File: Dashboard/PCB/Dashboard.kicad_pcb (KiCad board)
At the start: 4 copper layers, 95.9 x 92.1 mm, 90 parts, among them J1 Display, J2 Conn_01x26_Female, J3 LED, J7 PROGRAMMER, SW1 SW_SPST, U1 STM32F767ZIT6, U10 24LC01, U3 MP2359DJ-LF-Z, U4 AS4C1M16S-6TCN, U5 AT25SF128A-SHB-T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

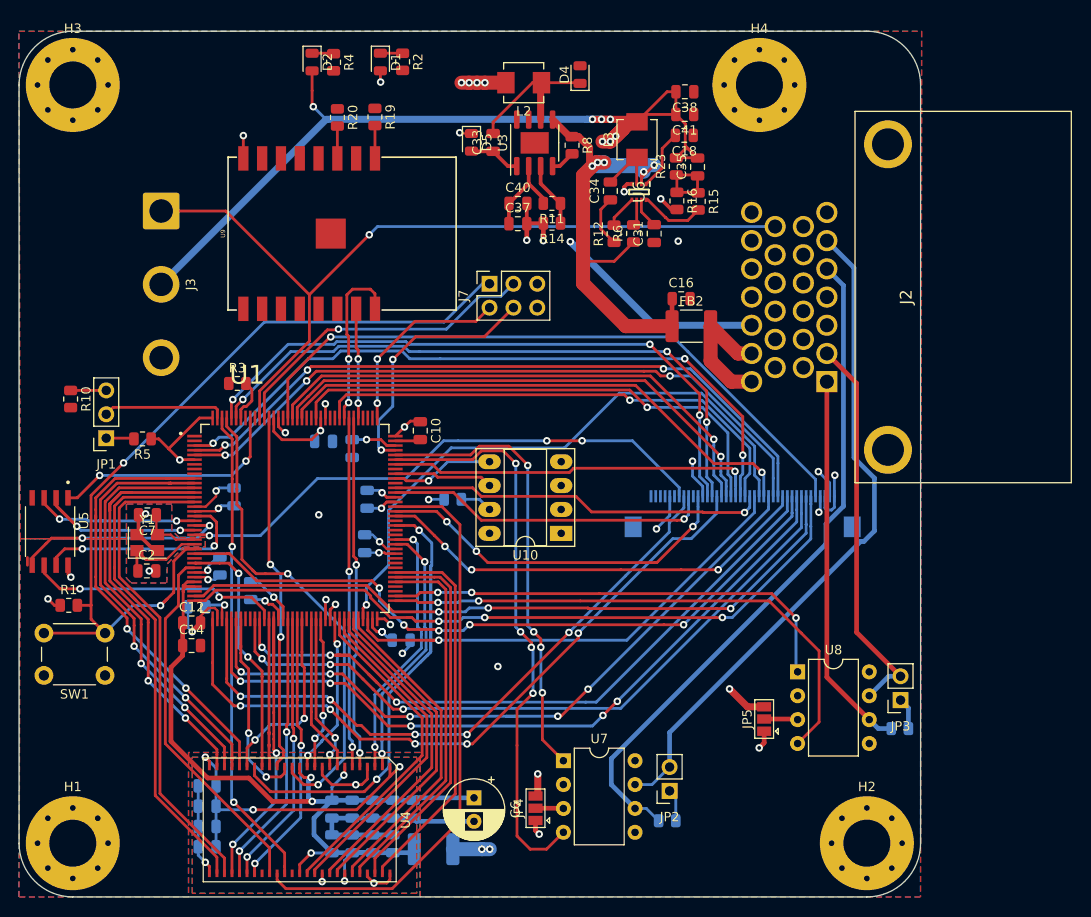
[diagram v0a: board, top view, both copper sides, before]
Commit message: Add signal led
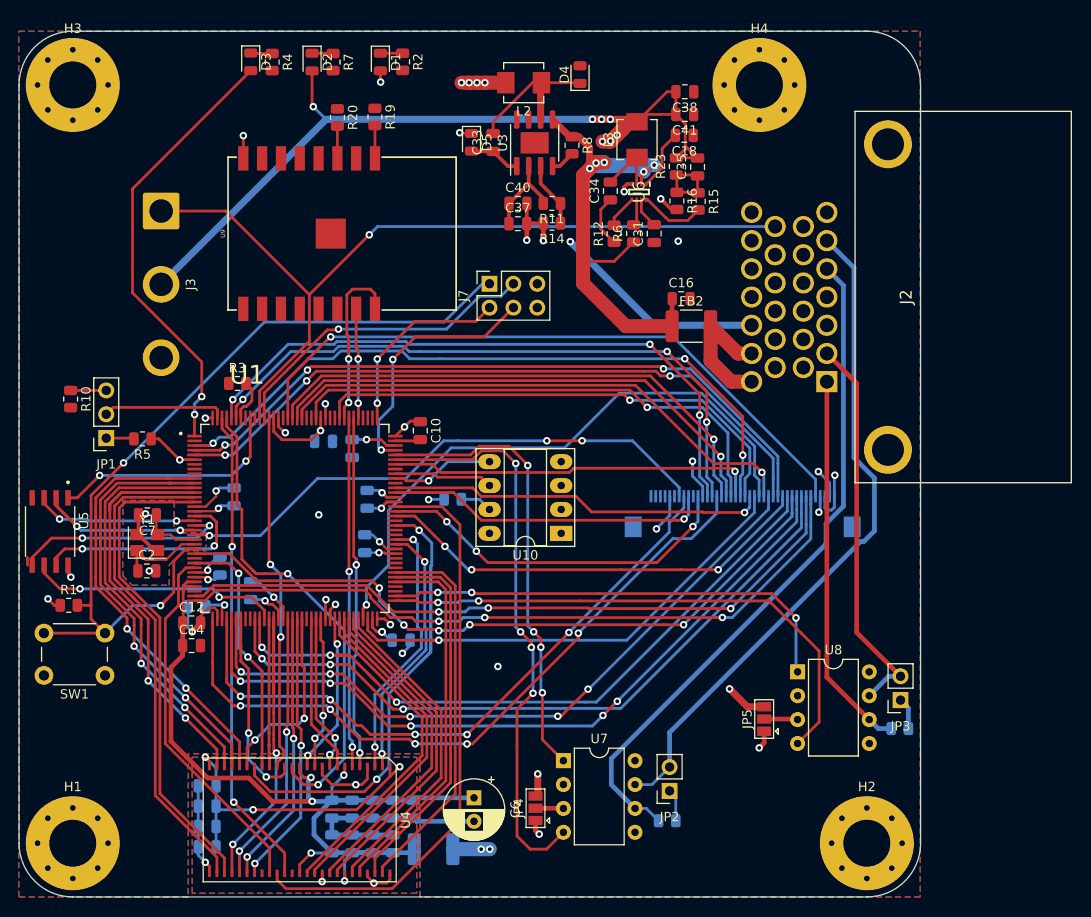
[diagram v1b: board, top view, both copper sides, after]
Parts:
- added D3: LED_5V, LED_SMD:LED_0805_2012Metric, F.Cu at (121.8, 32.5)
- added R7: R, Resistor_SMD:R_0805_2012Metric, F.Cu at (130.6, 32.5)
- moved R4 6.53 mm to (124.1, 32.5)
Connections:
- R4 pad 1: Net-(D2-Pad1) -> Net-(D3-Pad1)
- U1 pad 1: Net-(U1-Pad1) -> SIGNAL_LED
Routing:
- net SIGNAL_LED: track 0.00 -> 47.5 mm, vias 0 -> 2
- net +3V3: track 119.0 -> 113.7 mm, vias 30 -> 31
- net Net-(D3-Pad1): track 0.00 -> 2.31 mm

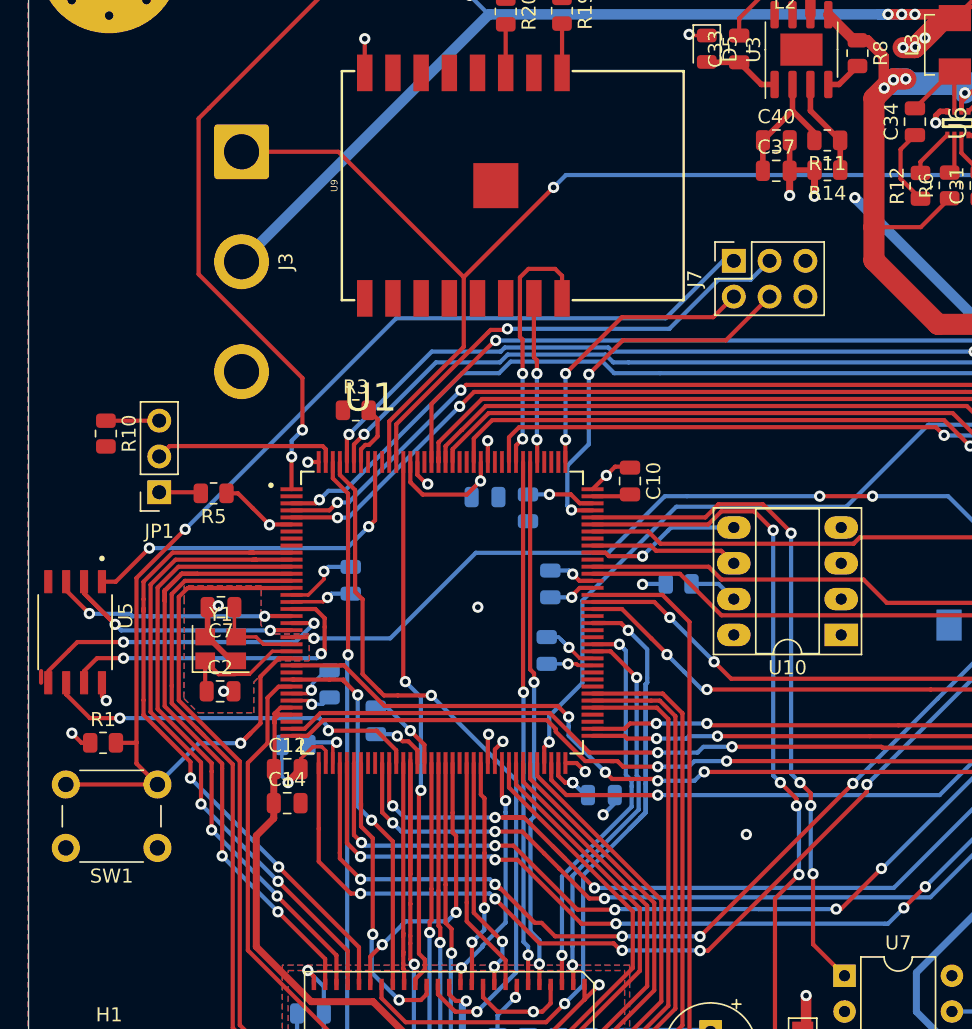
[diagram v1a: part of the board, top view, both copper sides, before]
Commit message: Add usb C to board
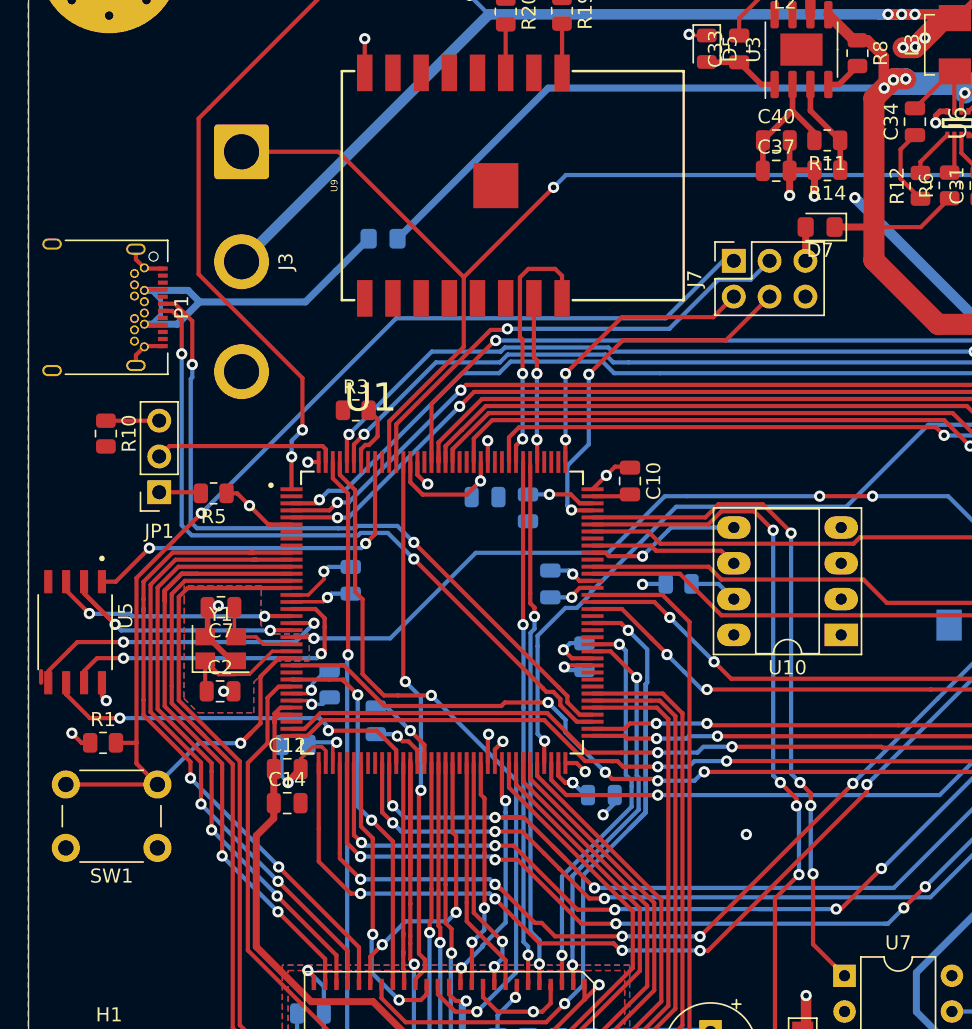
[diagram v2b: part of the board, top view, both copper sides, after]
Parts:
- added D6: D_Schottky, Diode_SMD:D_0805_2012Metric_Pad1.15x1.40mm_HandSolder, B.Cu at (122.3, 54.5)
- added D7: D_Schottky, Diode_SMD:D_0805_2012Metric_Pad1.15x1.40mm_HandSolder, F.Cu at (153.3, 53.7)
- added P1: USB_C_Plug, Connector_USB:USB_C_Receptacle_Amphenol_12401548E4-2A, F.Cu at (101.7, 59.4)
- moved C1 2.71 mm to (136.6, 84.2)
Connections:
- J7 pad 5: GND -> Net-(D7-Pad2)
- U1 pad 75: Net-(U1-Pad75) -> USB_OTG_DM
- U1 pad 76: Net-(U1-Pad76) -> USB_OTG_DP
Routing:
- net USB_OTG_DP: track 0.00 -> 51.5 mm, vias 0 -> 2
- net USB_OTG_DM: track 0.00 -> 51.5 mm, vias 0 -> 2
- net +12L: track 59.8 -> 101.6 mm
- net Net-(D6-Pad2): track 0.00 -> 29.4 mm
- net GND: track 122.4 -> 128.5 mm, vias 25 -> 24
- net Net-(D7-Pad2): track 0.00 -> 2.41 mm
- net /LTDC_G4: track 64.6 -> 65.5 mm
- net +3V3: track 113.7 -> 113.0 mm
- net /QUADSPI_NCS: track 25.3 -> 25.9 mm

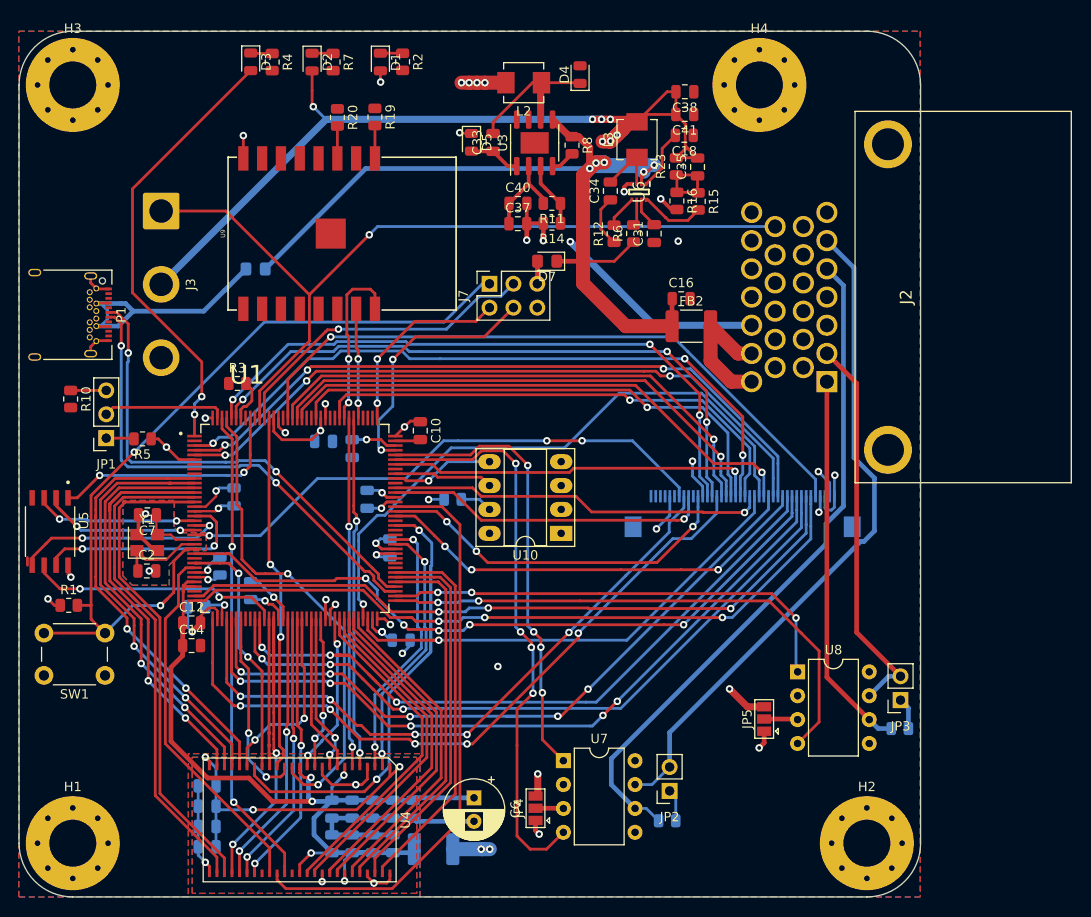
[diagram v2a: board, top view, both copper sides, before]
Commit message: Add reset and pd pin to esp
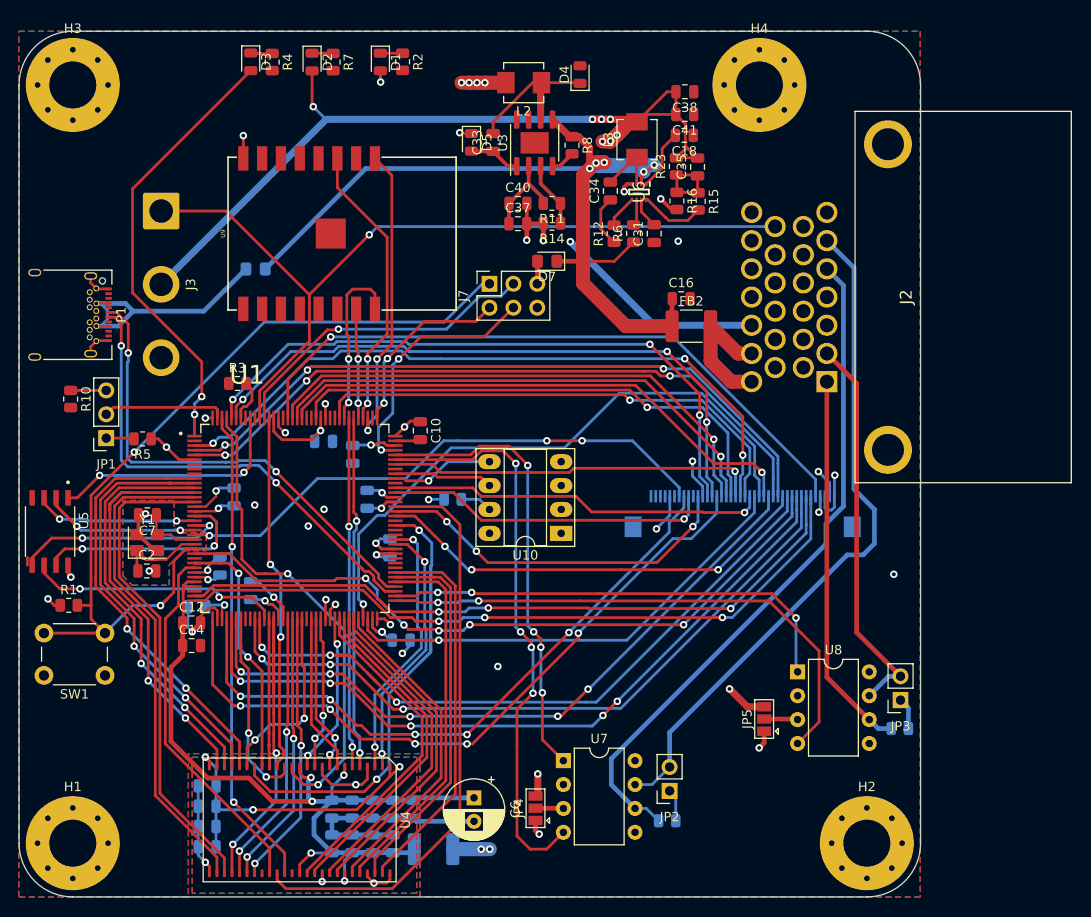
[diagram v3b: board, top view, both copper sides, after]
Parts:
- removed R19, R20: 10k, Resistor_SMD:R_0805_2012Metric
- moved C17 0.62 mm to (132.6, 74.2)
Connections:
- U1 pad 111: Net-(U1-Pad111) -> ESP_RESET
- U1 pad 112: Net-(U1-Pad112) -> ESP_EN
- U9 pad 1: Net-(R19-Pad2) -> ESP_RESET
- U9 pad 3: Net-(R20-Pad2) -> ESP_EN
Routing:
- net ESP_RESET: track 0.00 -> 32.1 mm, vias 0 -> 2
- net ESP_EN: track 0.00 -> 30.9 mm, vias 0 -> 2
- net Net-(R19-Pad2): track 3.50 -> 0.00 mm
- net Net-(R20-Pad2): track 3.44 -> 0.00 mm
- net CAN_H1: track 71.8 -> 72.5 mm
- net SWDCLK: track 20.5 -> 19.9 mm
- net GND: vias 24 -> 28

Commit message: Switch footprints of converter
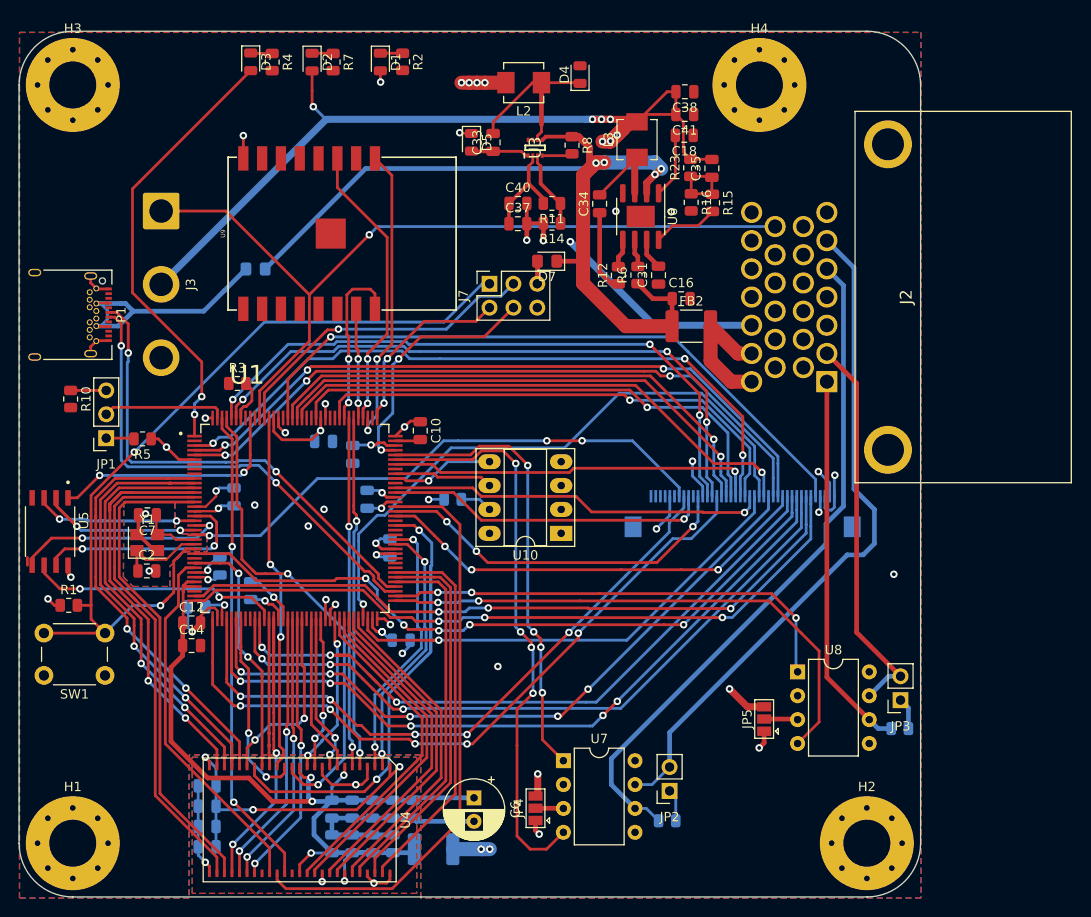
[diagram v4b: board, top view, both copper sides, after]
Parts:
- U3: footprint Package_SO:SOIC-8-1EP_3.9x4.9mm_P1.27mm_EP2.29x3mm -> SOT-583:SOTFL50P160X60-8N
- U6: footprint SOT-583:SOTFL50P160X60-8N -> Package_SO:SOIC-8-1EP_3.9x4.9mm_P1.27mm_EP2.29x3mm
- moved R6 4.44 mm to (163.0, 55.1)
- moved C31 4.44 mm to (165.2, 55.2)
- moved R12 4.44 mm to (160.9, 55.2)
- moved U6 2.62 mm to (163.3, 48.9)
- moved C34 1.78 mm to (158.9, 47.6)
- moved C35 1.53 mm to (170.8, 43.8)
- moved R15 1.53 mm to (170.9, 47.5)
- moved R16 1.53 mm to (168.6, 47.4)
- moved R23 1.53 mm to (168.6, 43.7)
- moved U3 0.52 mm to (152.0, 41.6)
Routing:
- net +12L: track 101.6 -> 94.6 mm, vias 5 -> 4
- net +5V: track 255.2 -> 251.7 mm
- net Net-(C34-Pad1): track 5.52 -> 8.80 mm
- net Net-(C34-Pad2): track 6.76 -> 9.75 mm
- net Net-(C33-Pad2): track 16.2 -> 18.5 mm
- net GND: track 128.5 -> 126.2 mm, vias 28 -> 27
- net Net-(R11-Pad1): track 6.95 -> 8.20 mm
- net Net-(C33-Pad1): track 5.48 -> 6.22 mm
- net Net-(R8-Pad2): track 2.61 -> 3.25 mm

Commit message: Add LED Driver
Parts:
- added C32: 100nF, Capacitor_SMD:C_0805_2012Metric, F.Cu at (180.3, 88.6)
- added G***: LOGO, PGR_logo:calliper, F.Cu at (178.3, 117.2)
- added Q1: Q_NMOS_GDS, Package_TO_SOT_SMD:SOT-89-3_Handsoldering, F.Cu at (178.1, 79.3)
- added R13: R, Resistor_SMD:R_0805_2012Metric, F.Cu at (176.5, 85.7)
- added R20: 1R, Resistor_SMD:R_0805_2012Metric, B.Cu at (183.4, 73.5)
- added R9: R, Resistor_SMD:R_0805_2012Metric, F.Cu at (180.2, 86.7)
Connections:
- J1 pad 1: GND -> DISPLAY_LED-
- J1 pad 2: +5V -> DISPLAY_LED+
- R16 pad 2: GND -> Net-(R16-Pad2)
- U1 pad 27: Net-(U1-Pad27) -> LED_CURRENT_SENSE
- U1 pad 81: Net-(U1-Pad81) -> LED_PWM
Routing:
- net LED_CURRENT_SENSE: track 0.00 -> 70.7 mm, vias 0 -> 6
- net +12L: track 94.6 -> 136.2 mm, vias 4 -> 6
- net LED_PWM: track 0.00 -> 40.3 mm, vias 0 -> 2
- net +5V: track 251.7 -> 216.5 mm, vias 11 -> 10
- net DISPLAY_LED-: track 0.00 -> 14.0 mm, vias 0 -> 1
- net DISPLAY_LED+: track 0.00 -> 12.5 mm, vias 0 -> 1
- net /FMC_BA0: track 59.7 -> 49.9 mm
- net Net-(Q1-Pad1): track 0.00 -> 3.30 mm
- net GND: track 126.2 -> 129.1 mm
- net /FMC_NBL0: track 51.5 -> 50.5 mm
- net /FMC_D0: track 28.0 -> 28.6 mm
